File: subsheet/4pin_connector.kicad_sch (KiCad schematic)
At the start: 3 parts, among them J1101 Conn_01x04, J1102 Conn_01x04, U1101 D1213A-04TS-7

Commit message: Position final few components
Removed one ESD diode arrray - experimental board, so not really needed,
with the exception of the USB lines.

Add and position 5V indicator LED

Finished wiring up the 5V buck-boost regulator
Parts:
- U1101: now not fitted; now left out of the parts list
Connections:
- net +5V: now reaches J1101.2 (Pin_2), J1102.2 (Pin_2)
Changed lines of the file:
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@@
 		(color 0 0 0 0)
 	)
+	(junction
+		(at 116.84 109.22)
+		(diameter 0)
+		(color 0 0 0 0)
+	)
 	(wire
 		(pts
@@
 		(pts
 			(xy 109.22 137.16) (xy 104.14 137.16)
+		)
+		(stroke
+			(width 0)
+			(type default)
+		)
+	)
+	(wire
+		(pts
+			(xy 116.84 86.36) (xy 116.84 109.22)
 		)
 		(stroke
@@
 				(path "/45b6f84a-e69b-48be-a49b-bc68872e2c15/85479e45-442b-480f-b0b0-1d208a9e4cfc"
 					(reference "J1101")
+					(unit 1)
+				)
+			)
+		)
+	)
+	(symbol
+		(lib_id "power:+5V")
+		(at 116.84 86.36 0)
+		(unit 1)
+		(exclude_from_sim no)
+		(in_bom yes)
+		(on_board yes)
+		(dnp no)
+		(fields_autoplaced yes)
+		(property "Reference" "#PWR01105"
+			(at 116.84 90.17 0)
+			(effects
+				(font
+					(size 1.27 1.27)
+				)
+				(hide yes)
+			)
+		)
+		(property "Value" "+5V"
+			(at 116.84 81.28 0)
+			(effects
+				(font
+					(size 1.27 1.27)
+				)
+			)
+		)
+		(property "Footprint" ""
+			(at 116.84 86.36 0)
+			(effects
+				(font
+					(size 1.27 1.27)
+				)
+				(hide yes)
+			)
+		)
+		(property "Datasheet" ""
+			(at 116.84 86.36 0)
+			(effects
+				(font
+					(size 1.27 1.27)
+				)
+				(hide yes)
+			)
+		)
+		(property "Description" "Power symbol creates a global label with name \"+5V\""
+			(at 116.84 86.36 0)
+			(effects
+				(font
+					(size 1.27 1.27)
+				)
+				(hide yes)
+			)
+		)
+		(pin "1"
+		)
+		(instances
+			(project "ESP_bare_chip_test_board"
+				(path "/45b6f84a-e69b-48be-a49b-bc68872e2c15/85479e45-442b-480f-b0b0-1d208a9e4cfc"
+					(reference "#PWR01105")
 					(unit 1)
 				)
@@
 		(at 99.06 127 0)
 		(unit 1)
-		(exclude_from_sim no)
-		(in_bom yes)
-		(on_board yes)
-		(dnp no)
+		(exclude_from_sim yes)
+		(in_bom no)
+		(on_board no)
+		(dnp yes)
 		(fields_autoplaced yes)
 		(property "Reference" "U1101"

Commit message: Add JLCPCB corrections for new components
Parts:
- J1101: JLCPCB_IGNORE (none) -> 1
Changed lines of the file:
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@@
 			)
 		)
-		(property "JLCPCB_IGNORE" ""
+		(property "JLCPCB_IGNORE" "1"
 			(at 121.92 152.4 0)
 			(effects

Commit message: Silkscreen work. Edit tittle block/version number
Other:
- company: (c) -> (c) Vincent Dalstra
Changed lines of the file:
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@@
 	(title_block
 		(title "Untitled 4-layer JLCPCB")
-		(date "1984/04/01")
-		(rev "v1.0.0")
-		(company "(c)")
+		(date "2024-06-14")
+		(rev "1.0.0")
+		(company "(c) Vincent Dalstra")
 	)
 	(junction

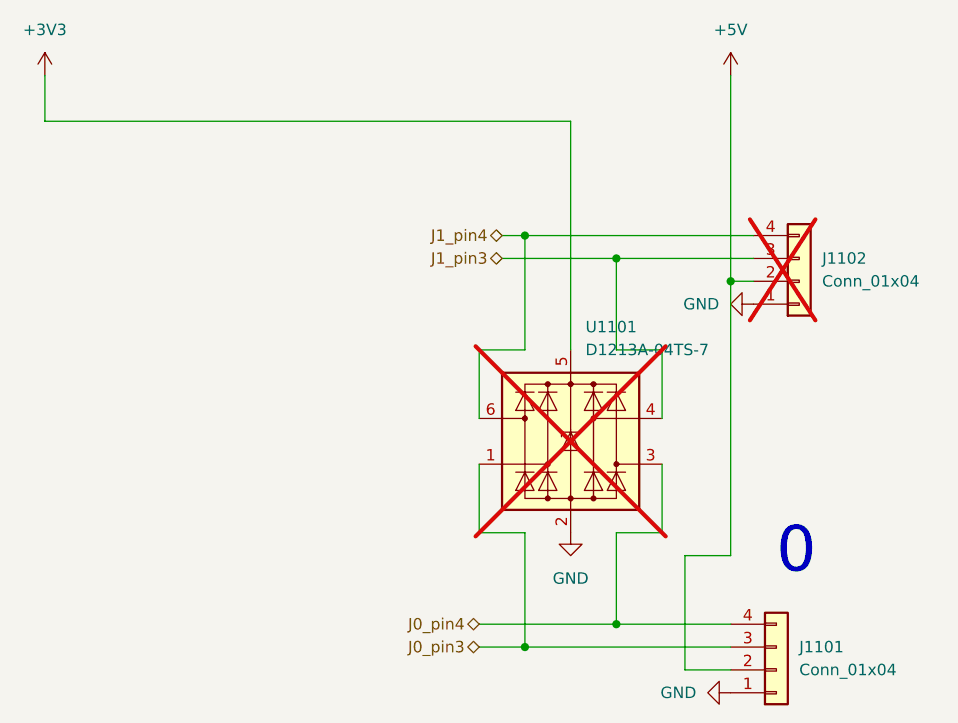
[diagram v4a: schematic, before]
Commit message: Move all subsheets into 'main' subsheet, below root
Keeping all the subsheets in a dedicated 'subsheet' folder makes things
much, much neater. However, specifying filepaths for subsheets has an
interesting problem; they use paths RELATIVE TO THE PARENT SHEET.

The consequence of is that if a subsheet is part of the root sheet, it
needs to be prefixed with 'subsheet/', but NOT if it's further down.
This inconsistency can be resolved by having a single 'main' sheet at
the top that doesn't move.

It's also useful to have a top-level space to put down changelogs,
descriptions etc.
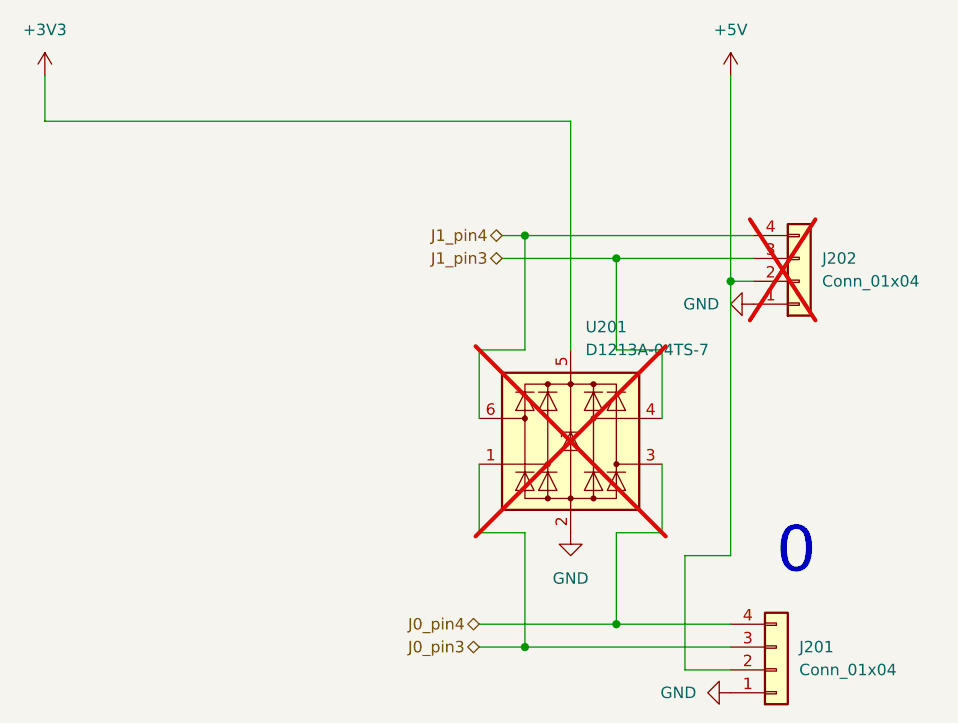
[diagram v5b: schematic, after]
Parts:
- renumbered J1101 to J201, J1102 to J202, U1101 to U201
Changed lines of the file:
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@@
 		(shape bidirectional)
 		(at 91.44 104.14 180)
-		(fields_autoplaced yes)
 		(effects
 			(font
@@
 		(shape bidirectional)
 		(at 88.9 149.86 180)
-		(fields_autoplaced yes)
 		(effects
 			(font
@@
 		(shape bidirectional)
 		(at 91.44 106.68 180)
-		(fields_autoplaced yes)
 		(effects
 			(font
@@
 		(shape bidirectional)
 		(at 88.9 147.32 180)
-		(fields_autoplaced yes)
 		(effects
 			(font
@@
 		(on_board yes)
 		(dnp no)
-		(property "Reference" "J1101"
+		(property "Reference" "J201"
 			(at 124.46 149.86 0)
 			(effects
@@
 		(instances
 			(project "ESP_bare_chip_test_board"
-				(path "/45b6f84a-e69b-48be-a49b-bc68872e2c15/85479e45-442b-480f-b0b0-1d208a9e4cfc"
-					(reference "J1101")
+				(path "/45b6f84a-e69b-48be-a49b-bc68872e2c15/f48098a1-cacc-4192-b650-2a34a2ba76dc/95cbd5d6-5cb3-4431-8459-ab3e7dc12be6"
+					(reference "J201")
 					(unit 1)
 				)
@@
 		(dnp no)
 		(fields_autoplaced yes)
-		(property "Reference" "#PWR01105"
+		(property "Reference" "#PWR203"
 			(at 116.84 90.17 0)
 			(effects
@@
 		(instances
 			(project "ESP_bare_chip_test_board"
-				(path "/45b6f84a-e69b-48be-a49b-bc68872e2c15/85479e45-442b-480f-b0b0-1d208a9e4cfc"
-					(reference "#PWR01105")
+				(path "/45b6f84a-e69b-48be-a49b-bc68872e2c15/f48098a1-cacc-4192-b650-2a34a2ba76dc/95cbd5d6-5cb3-4431-8459-ab3e7dc12be6"
+					(reference "#PWR203")
 					(unit 1)
 				)
@@
 		(dnp no)
 		(fields_autoplaced yes)
-		(property "Reference" "#PWR01104"
+		(property "Reference" "#PWR205"
 			(at 113.03 111.76 0)
 			(effects
@@
 		(instances
 			(project "ESP_bare_chip_test_board"
-				(path "/45b6f84a-e69b-48be-a49b-bc68872e2c15/85479e45-442b-480f-b0b0-1d208a9e4cfc"
-					(reference "#PWR01104")
+				(path "/45b6f84a-e69b-48be-a49b-bc68872e2c15/f48098a1-cacc-4192-b650-2a34a2ba76dc/95cbd5d6-5cb3-4431-8459-ab3e7dc12be6"
+					(reference "#PWR205")
 					(unit 1)
 				)
@@
 		(on_board no)
 		(dnp yes)
-		(property "Reference" "J1102"
+		(property "Reference" "J202"
 			(at 127 106.68 0)
 			(effects
@@
 		(instances
 			(project "ESP_bare_chip_test_board"
-				(path "/45b6f84a-e69b-48be-a49b-bc68872e2c15/85479e45-442b-480f-b0b0-1d208a9e4cfc"
-					(reference "J1102")
+				(path "/45b6f84a-e69b-48be-a49b-bc68872e2c15/f48098a1-cacc-4192-b650-2a34a2ba76dc/95cbd5d6-5cb3-4431-8459-ab3e7dc12be6"
+					(reference "J202")
 					(unit 1)
 				)
@@
 		(on_board yes)
 		(dnp no)
-		(property "Reference" "#PWR01103"
+		(property "Reference" "#PWR204"
 			(at 110.49 154.94 0)
 			(effects
@@
 		(instances
 			(project "ESP_bare_chip_test_board"
-				(path "/45b6f84a-e69b-48be-a49b-bc68872e2c15/85479e45-442b-480f-b0b0-1d208a9e4cfc"
-					(reference "#PWR01103")
+				(path "/45b6f84a-e69b-48be-a49b-bc68872e2c15/f48098a1-cacc-4192-b650-2a34a2ba76dc/95cbd5d6-5cb3-4431-8459-ab3e7dc12be6"
+					(reference "#PWR204")
 					(unit 1)
 				)
@@
 		(dnp no)
 		(fields_autoplaced yes)
-		(property "Reference" "#PWR01101"
+		(property "Reference" "#PWR201"
 			(at 40.64 90.17 0)
 			(effects
@@
 		(instances
 			(project "ESP_bare_chip_test_board"
-				(path "/45b6f84a-e69b-48be-a49b-bc68872e2c15/85479e45-442b-480f-b0b0-1d208a9e4cfc"
-					(reference "#PWR01101")
+				(path "/45b6f84a-e69b-48be-a49b-bc68872e2c15/f48098a1-cacc-4192-b650-2a34a2ba76dc/95cbd5d6-5cb3-4431-8459-ab3e7dc12be6"
+					(reference "#PWR201")
 					(unit 1)
 				)
@@
 		(dnp yes)
 		(fields_autoplaced yes)
-		(property "Reference" "U1101"
+		(property "Reference" "U201"
 			(at 100.7111 114.3 0)
 			(effects
@@
 		(instances
 			(project "ESP_bare_chip_test_board"
-				(path "/45b6f84a-e69b-48be-a49b-bc68872e2c15/85479e45-442b-480f-b0b0-1d208a9e4cfc"
-					(reference "U1101")
+				(path "/45b6f84a-e69b-48be-a49b-bc68872e2c15/f48098a1-cacc-4192-b650-2a34a2ba76dc/95cbd5d6-5cb3-4431-8459-ab3e7dc12be6"
+					(reference "U201")
 					(unit 1)
 				)
@@
 		(dnp no)
 		(fields_autoplaced yes)
-		(property "Reference" "#PWR01102"
+		(property "Reference" "#PWR202"
 			(at 99.06 143.51 0)
 			(effects
@@
 		(instances
 			(project "ESP_bare_chip_test_board"
-				(path "/45b6f84a-e69b-48be-a49b-bc68872e2c15/85479e45-442b-480f-b0b0-1d208a9e4cfc"
-					(reference "#PWR01102")
-					(unit 1)
-				)
+				(path "/45b6f84a-e69b-48be-a49b-bc68872e2c15/f48098a1-cacc-4192-b650-2a34a2ba76dc/95cbd5d6-5cb3-4431-8459-ab3e7dc12be6"
+					(reference "#PWR202")
+					(unit 1)
+				)
